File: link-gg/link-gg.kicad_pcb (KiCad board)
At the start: 2 copper layers, 31.8 x 25.4 mm, 2 parts, among them J1 Mini-DIN-8, J2 DE9_Pins_MountingHoles

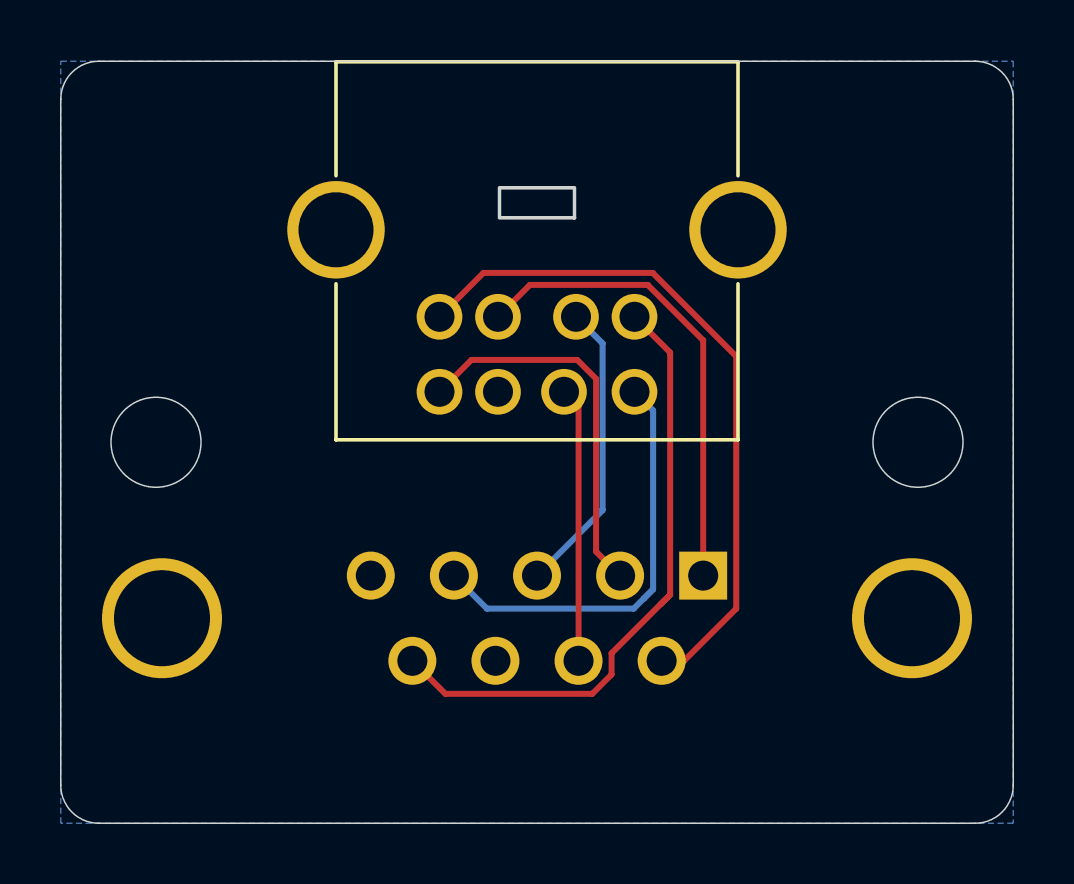
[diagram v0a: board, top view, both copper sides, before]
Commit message: Use M3 mounting screw footprint
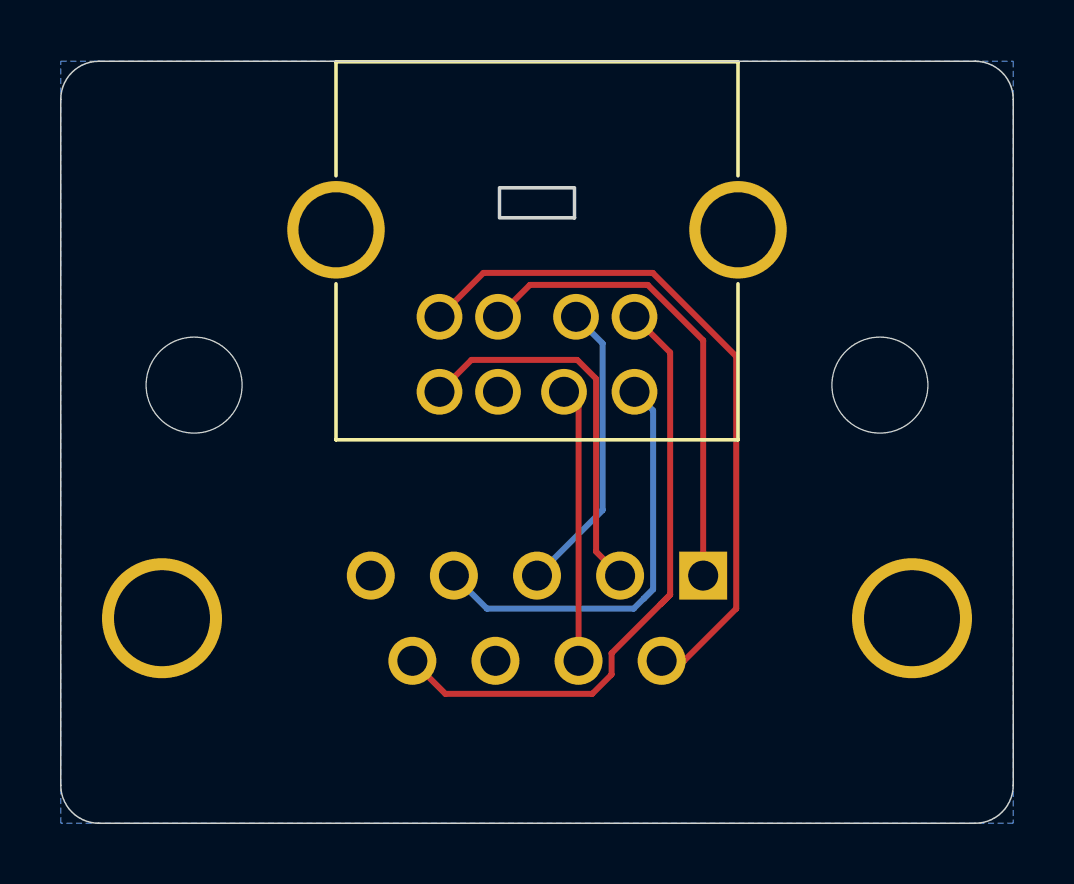
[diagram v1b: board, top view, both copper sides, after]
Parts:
- added REF**: MountingHole_3.2mm_M3, MountingHole:MountingHole_3.2mm_M3, B.Cu at (93.3, 118.7)
- added REF**: MountingHole_3.2mm_M3, MountingHole:MountingHole_3.2mm_M3, B.Cu at (116.2, 118.7)
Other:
- outline, holes or cut-outs redrawn
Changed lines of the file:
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@@
+		(embedded_fonts no)
+	)
+	(footprint "MountingHole:MountingHole_3.2mm_M3"
+		(layer "B.Cu")
+		(at 93.345 118.745 180)
+		(descr "Mounting Hole 3.2mm, M3, no annular, generated by kicad-footprint-generator mountinghole.py")
+		(tags "mountinghole M3")
+		(property "Reference" "REF**"
+			(at 0 4.15 0)
+			(layer "B.SilkS")
+			(hide yes)
+			(effects
+				(font
+					(size 1 1)
+					(thickness 0.15)
+				)
+				(justify mirror)
+			)
+		)
+		(property "Value" "MountingHole_3.2mm_M3"
+			(at 0 -4.15 0)
+			(layer "B.Fab")
+			(hide yes)
+			(effects
+				(font
+					(size 1 1)
+					(thickness 0.15)
+				)
+				(justify mirror)
+			)
+		)
+		(property "Datasheet" ""
+			(at 0 0 0)
+			(layer "B.Fab")
+			(hide yes)
+			(effects
+				(font
+					(size 1.27 1.27)
+					(thickness 0.15)
+				)
+				(justify mirror)
+			)
+		)
+		(property "Description" ""
+			(at 0 0 0)
+			(layer "B.Fab")
+			(hide yes)
+			(effects
+				(font
+					(size 1.27 1.27)
+					(thickness 0.15)
+				)
+				(justify mirror)
+			)
+		)
+		(attr board_only exclude_from_pos_files exclude_from_bom)
+		(fp_circle
+			(center 0 0)
+			(end 3.2 0)
+			(stroke
+				(width 0.15)
+				(type solid)
+			)
+			(fill no)
+			(layer "Cmts.User")
+		)
+		(fp_circle
+			(center 0 0)
+			(end 3.45 0)
+			(stroke
+				(width 0.05)
+				(type solid)
+			)
+			(fill no)
+			(layer "B.CrtYd")
+		)
+		(pad "" np_thru_hole circle
+			(at 0 0 180)
+			(size 3.2 3.2)
+			(drill 3.2)
+			(layers "*.Cu" "*.Mask")
+		)
+		(embedded_fonts no)
+	)
+	(footprint "MountingHole:MountingHole_3.2mm_M3"
+		(layer "B.Cu")
+		(at 116.205 118.745 180)
+		(descr "Mounting Hole 3.2mm, M3, no annular, generated by kicad-footprint-generator mountinghole.py")
+		(tags "mountinghole M3")
+		(property "Reference" "REF**"
+			(at 0 4.15 0)
+			(layer "B.SilkS")
+			(hide yes)
+			(effects
+				(font
+					(size 1 1)
+					(thickness 0.15)
+				)
+				(justify mirror)
+			)
+		)
+		(property "Value" "MountingHole_3.2mm_M3"
+			(at 0 -4.15 0)
+			(layer "B.Fab")
+			(hide yes)
+			(effects
+				(font
+					(size 1 1)
+					(thickness 0.15)
+				)
+				(justify mirror)
+			)
+		)
+		(property "Datasheet" ""
+			(at 0 0 0)
+			(layer "B.Fab")
+			(hide yes)
+			(effects
+				(font
+					(size 1.27 1.27)
+					(thickness 0.15)
+				)
+				(justify mirror)
+			)
+		)
+		(property "Description" ""
+			(at 0 0 0)
+			(layer "B.Fab")
+			(hide yes)
+			(effects
+				(font
+					(size 1.27 1.27)
+					(thickness 0.15)
+				)
+				(justify mirror)
+			)
+		)
+		(attr board_only exclude_from_pos_files exclude_from_bom)
+		(fp_circle
+			(center 0 0)
+			(end 3.2 0)
+			(stroke
+				(width 0.15)
+				(type solid)
+			)
+			(fill no)
+			(layer "Cmts.User")
+		)
+		(fp_circle
+			(center 0 0)
+			(end 3.45 0)
+			(stroke
+				(width 0.05)
+				(type solid)
+			)
+			(fill no)
+			(layer "B.CrtYd")
+		)
+		(pad "" np_thru_hole circle
+			(at 0 0 180)
+			(size 3.2 3.2)
+			(drill 3.2)
+			(layers "*.Cu" "*.Mask")
+		)
 		(embedded_fonts no)
 	)
@@
 		(layer "Edge.Cuts")
 	)
-	(gr_circle
-		(center 117.475 120.649999)
-		(end 118.975 120.649999)
-		(stroke
-			(width 0.05)
-			(type solid)
-		)
-		(fill no)
-		(layer "Edge.Cuts")
-	)
 	(gr_line
 		(start 88.899998 132.080001)
@@
 		(layer "Edge.Cuts")
 	)
-	(gr_circle
-		(center 92.075 120.65)
-		(end 93.575 120.65)
-		(stroke
-			(width 0.05)
-			(type solid)
-		)
-		(fill no)
-		(layer "Edge.Cuts")
-	)
